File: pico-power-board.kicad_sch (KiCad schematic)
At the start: 109 parts, among them J1 Conn_02x10_Counter_Clockwise, J10 Conn_01x20_Female, J2 Conn_02x10_Counter_Clockwise, J3 Conn_02x10_Counter_Clockwise, J4 Conn_02x10_Counter_Clockwise, J5 Conn_02x10_Counter_Clockwise, J6 Conn_02x10_Counter_Clockwise, J7 DC-042C-Z-2.5, J8 Conn_01x06_Male, J9 Conn_01x20_Female, U1 TMP112AIDRLR, U2 INA219AxD, U3 K7803-500R3, U4 74LVC1G125GW,125, U5 74LVC1G125GW,125, U6 74LVC1G125GW,125, U7 74LVC1G125GW,125, U8 74LVC1G125GW,125, U9 74LVC1G125GW,125

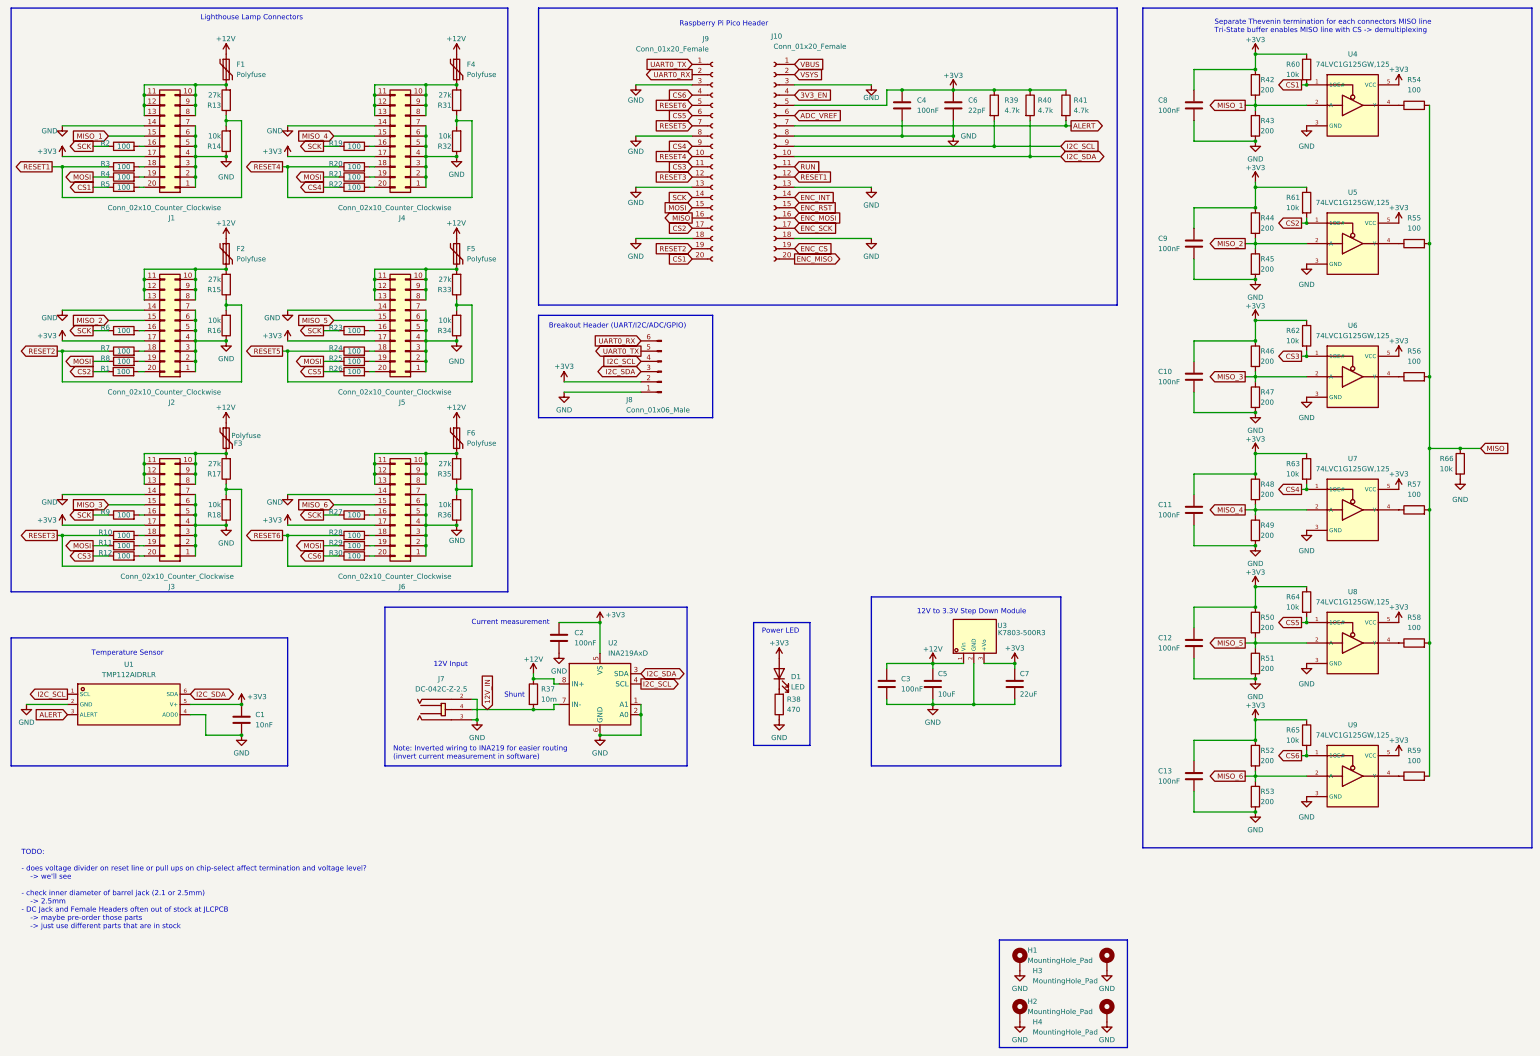
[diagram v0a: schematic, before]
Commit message: Fix wrong resistor 100k -> 100R, add teardrops, larger resistor to dim power led
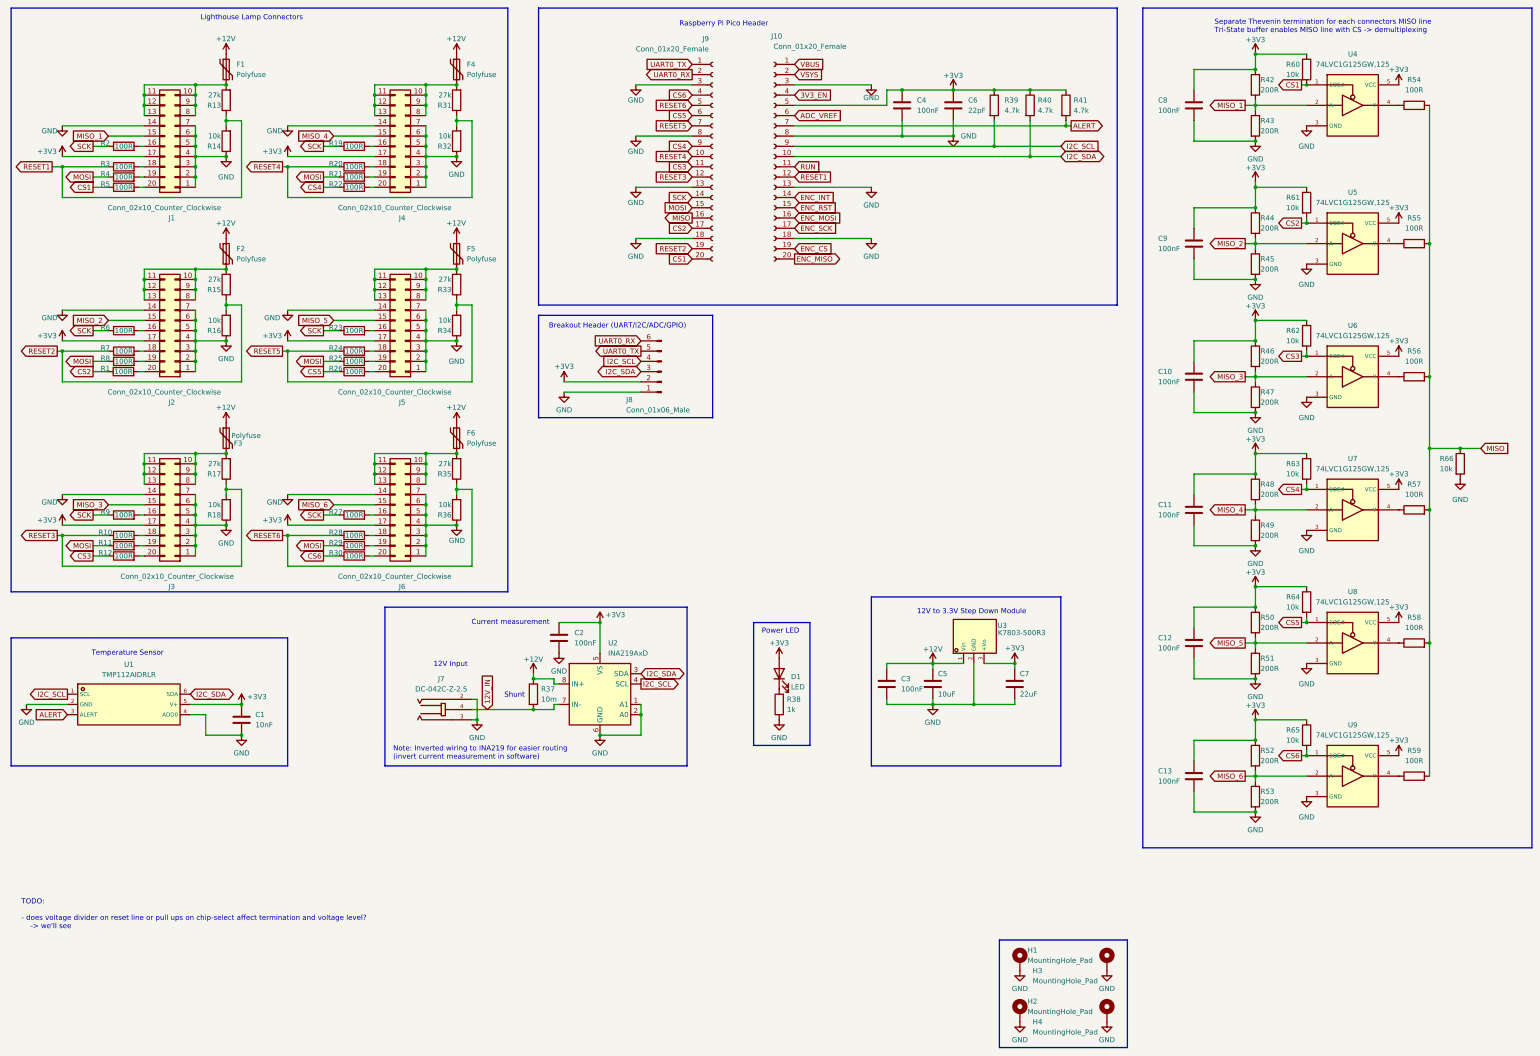
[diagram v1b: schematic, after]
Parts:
- F1, F2, F3, F4, F5, F6: LCSC C883135 -> C516068
- R1, R10, R11, R12, R19, R2, R20, R21, R22, R23, R24, R25, R26, R27, R28, R29, R3, R30, R4, R5, R54, R55, R56, R57, R58, R59, R6, R7, R8, R9: value 100 -> 100R; LCSC C881354 -> C86983
- R38: value 470 -> 1k; footprint Resistor_SMD:R_0805_2012Metric -> Resistor_SMD:R_0603_1608Metric; JLC 0805 -> 0603; LCSC C3152234 -> C2845198
- R42, R43, R44, R45, R46, R47, R48, R49, R50, R51, R52, R53: value 200 -> 200R
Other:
- note added: "TODO: - does voltage divider on reset line or pull ups on chip-select affect termination and voltage level? -> we'll see"
- note removed: "TODO: - does voltage divider on reset line or pull ups on chip-select affect termination and voltage level? -> we'll see - check inner diameter of barrel jack (2.1 or 2.5mm) -> 2.5mm - DC Jack and Female Headers often out of stock at JLCPCB -> maybe pre-order those parts -> just use different parts that are in stock"

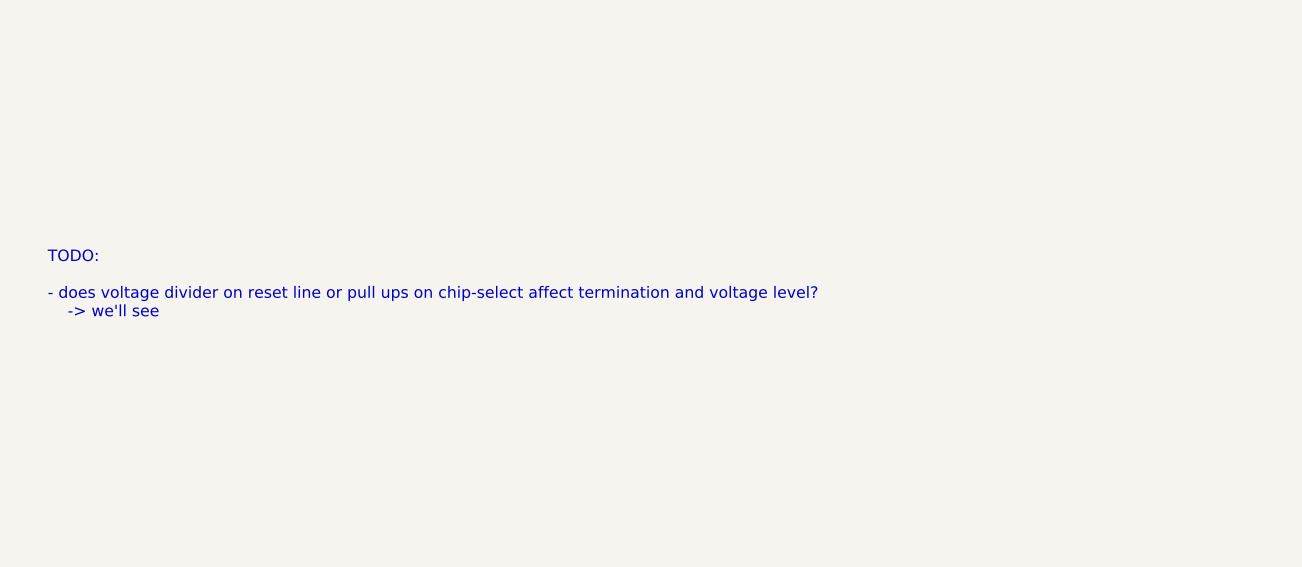
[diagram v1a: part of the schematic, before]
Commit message: Move pico down in order to not interfere with the case on the backside
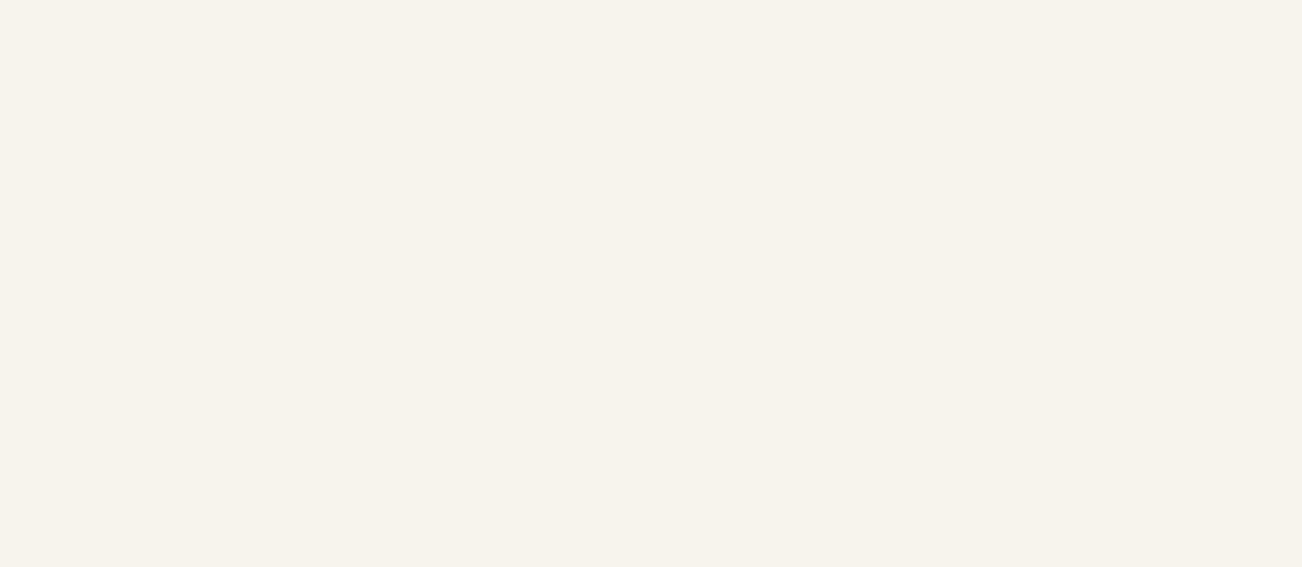
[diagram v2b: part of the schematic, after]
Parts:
- F1, F2, F3, F4, F5, F6: LCSC C516068 -> C883135
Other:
- note removed: "TODO: - does voltage divider on reset line or pull ups on chip-select affect termination and voltage level? -> we'll see"
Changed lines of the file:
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@@
     (effects (font (size 1.27 1.27)) (justify left bottom))
   )
-  (text "TODO:\n\n- does voltage divider on reset line or pull ups on chip-select affect termination and voltage level?\n	-> we'll see\n"
-    (at 22.86 254 0)
-    (effects (font (size 1.27 1.27)) (justify left bottom))
-  )
   (text "Lighthouse Lamp Connectors" (at 92.71 28.575 0)
     (effects (font (size 1.27 1.27)) (justify right bottom))
@@
       (effects (font (size 1.27 1.27)) (justify left) hide)
     )
-    (property "Datasheet" "https://datasheet.lcsc.com/lcsc/2007081813_Jinrui-Electronic-Materials-Co--JK-NSMD300L-12V_C516068.pdf" (at 73.66 132.08 0)
+    (property "Datasheet" "https://datasheet.lcsc.com/lcsc/2305121423_BHFUSE-BSMD1206-200-12V_C883135.pdf" (at 73.66 132.08 0)
       (effects (font (size 1.27 1.27)) hide)
     )
@@
       (effects (font (size 1.27 1.27)) hide)
     )
-    (property "LCSC" "C516068" (at 73.66 132.08 0)
+    (property "LCSC" "C883135" (at 73.66 132.08 0)
       (effects (font (size 1.27 1.27)) hide)
     )
@@
       (effects (font (size 1.27 1.27)) (justify left) hide)
     )
-    (property "Datasheet" "https://datasheet.lcsc.com/lcsc/2007081813_Jinrui-Electronic-Materials-Co--JK-NSMD300L-12V_C516068.pdf" (at 130.81 40.64 0)
+    (property "Datasheet" "https://datasheet.lcsc.com/lcsc/2305121423_BHFUSE-BSMD1206-200-12V_C883135.pdf" (at 130.81 40.64 0)
       (effects (font (size 1.27 1.27)) hide)
     )
@@
       (effects (font (size 1.27 1.27)) hide)
     )
-    (property "LCSC" "C516068" (at 130.81 40.64 0)
+    (property "LCSC" "C883135" (at 130.81 40.64 0)
       (effects (font (size 1.27 1.27)) hide)
     )
@@
       (effects (font (size 1.27 1.27)) (justify left) hide)
     )
-    (property "Datasheet" "https://datasheet.lcsc.com/lcsc/2007081813_Jinrui-Electronic-Materials-Co--JK-NSMD300L-12V_C516068.pdf" (at 73.66 86.36 0)
+    (property "Datasheet" "https://datasheet.lcsc.com/lcsc/2305121423_BHFUSE-BSMD1206-200-12V_C883135.pdf" (at 73.66 86.36 0)
       (effects (font (size 1.27 1.27)) hide)
     )
@@
       (effects (font (size 1.27 1.27)) hide)
     )
-    (property "LCSC" "C516068" (at 73.66 86.36 0)
+    (property "LCSC" "C883135" (at 73.66 86.36 0)
       (effects (font (size 1.27 1.27)) hide)
     )
@@
       (effects (font (size 1.27 1.27)) (justify left) hide)
     )
-    (property "Datasheet" "https://datasheet.lcsc.com/lcsc/2007081813_Jinrui-Electronic-Materials-Co--JK-NSMD300L-12V_C516068.pdf" (at 130.81 132.08 0)
+    (property "Datasheet" "https://datasheet.lcsc.com/lcsc/2305121423_BHFUSE-BSMD1206-200-12V_C883135.pdf" (at 130.81 132.08 0)
       (effects (font (size 1.27 1.27)) hide)
     )
@@
       (effects (font (size 1.27 1.27)) hide)
     )
-    (property "LCSC" "C516068" (at 130.81 132.08 0)
+    (property "LCSC" "C883135" (at 130.81 132.08 0)
       (effects (font (size 1.27 1.27)) hide)
     )
@@
       (effects (font (size 1.27 1.27)) (justify left) hide)
     )
-    (property "Datasheet" "https://datasheet.lcsc.com/lcsc/2007081813_Jinrui-Electronic-Materials-Co--JK-NSMD300L-12V_C516068.pdf" (at 130.81 86.36 0)
+    (property "Datasheet" "https://datasheet.lcsc.com/lcsc/2305121423_BHFUSE-BSMD1206-200-12V_C883135.pdf" (at 130.81 86.36 0)
       (effects (font (size 1.27 1.27)) hide)
     )
@@
       (effects (font (size 1.27 1.27)) hide)
     )
-    (property "LCSC" "C516068" (at 130.81 86.36 0)
+    (property "LCSC" "C883135" (at 130.81 86.36 0)
       (effects (font (size 1.27 1.27)) hide)
     )
@@
       (effects (font (size 1.27 1.27)) (justify left) hide)
     )
-    (property "Datasheet" "https://datasheet.lcsc.com/lcsc/2007081813_Jinrui-Electronic-Materials-Co--JK-NSMD300L-12V_C516068.pdf" (at 73.66 40.64 0)
+    (property "Datasheet" "https://datasheet.lcsc.com/lcsc/2305121423_BHFUSE-BSMD1206-200-12V_C883135.pdf" (at 73.66 40.64 0)
       (effects (font (size 1.27 1.27)) hide)
     )
@@
       (effects (font (size 1.27 1.27)) hide)
     )
-    (property "LCSC" "C516068" (at 73.66 40.64 0)
+    (property "LCSC" "C883135" (at 73.66 40.64 0)
       (effects (font (size 1.27 1.27)) hide)
     )
